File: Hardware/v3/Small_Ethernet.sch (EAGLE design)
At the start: 56 parts, among them U1 EDISON_CONNECTOR_FULLMOUNTING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, U2 LAN9512-JZX, U3 MAX4995AAUT+, U4 EDISON_CONNECTOR_FULLHEADER, X1 J1011F01P

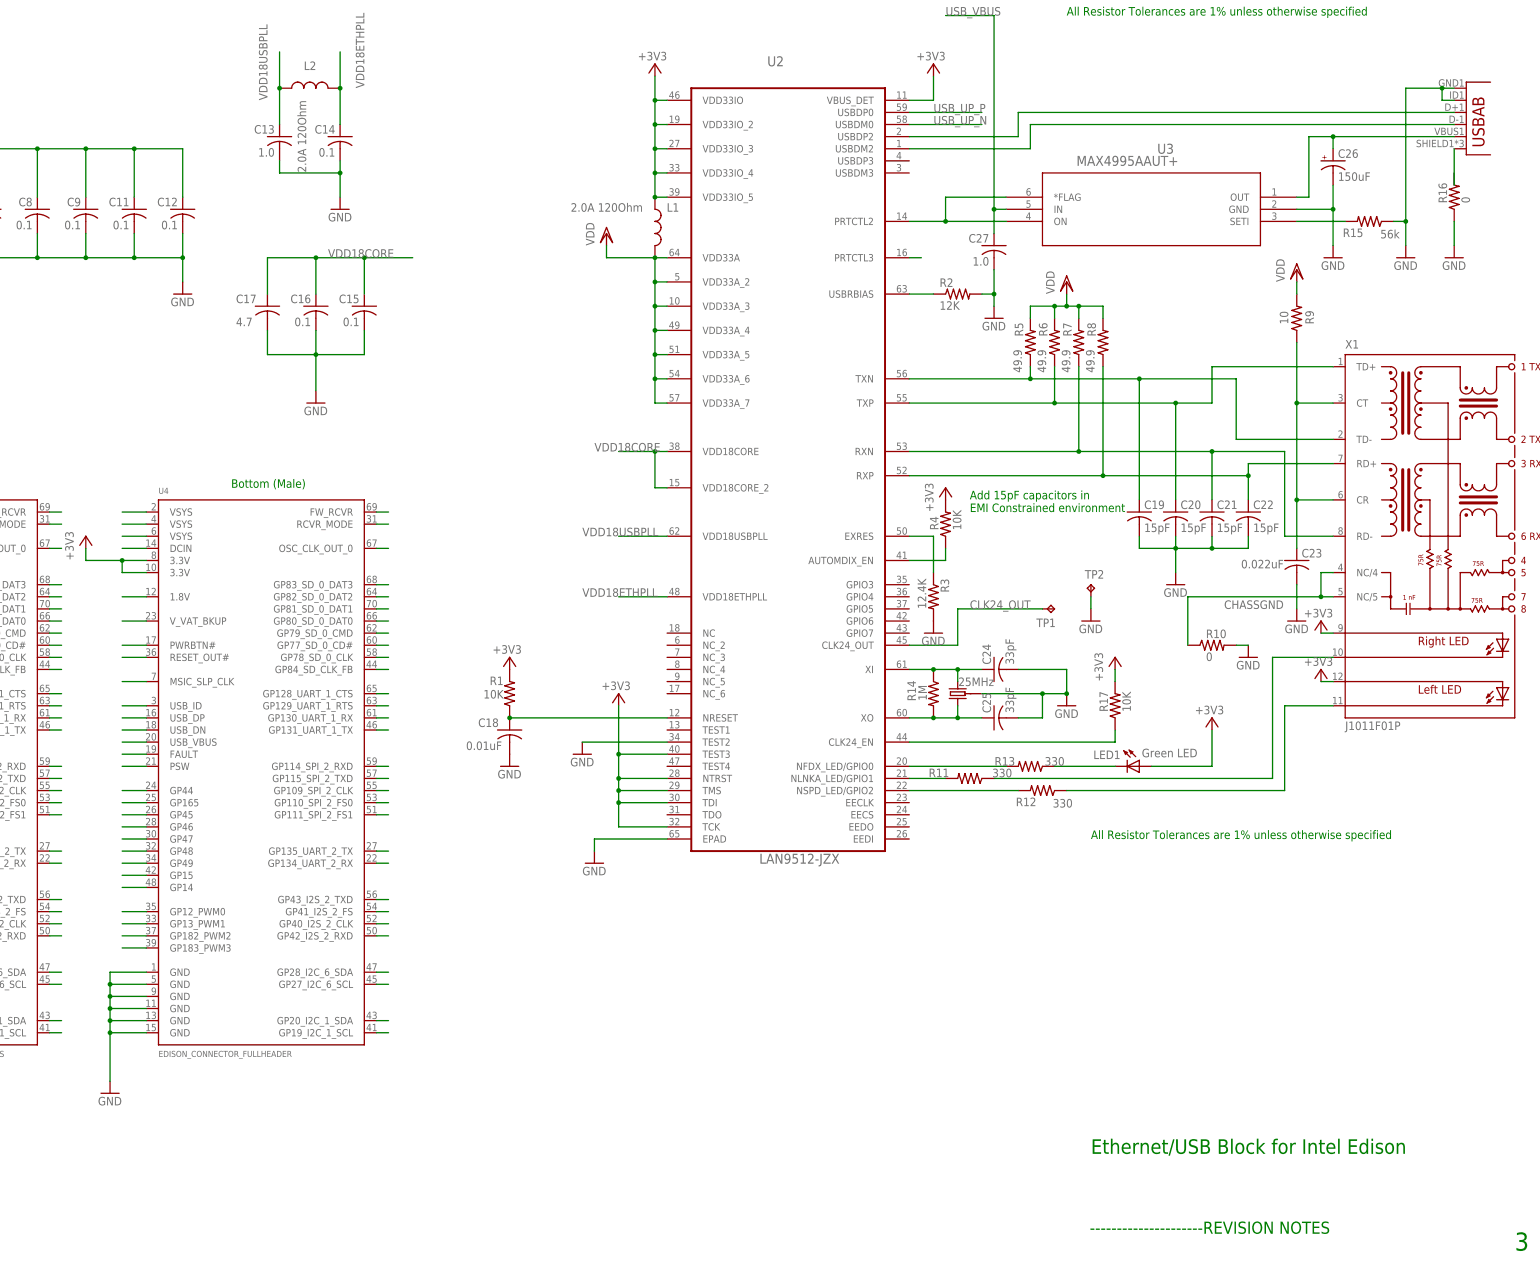
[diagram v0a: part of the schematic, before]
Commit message: Added ground fills. PoE: power planes around U7, diode for power through microB. Small: changed C26 to 2 caps, removed NP caps, removed test points, replaced crystal
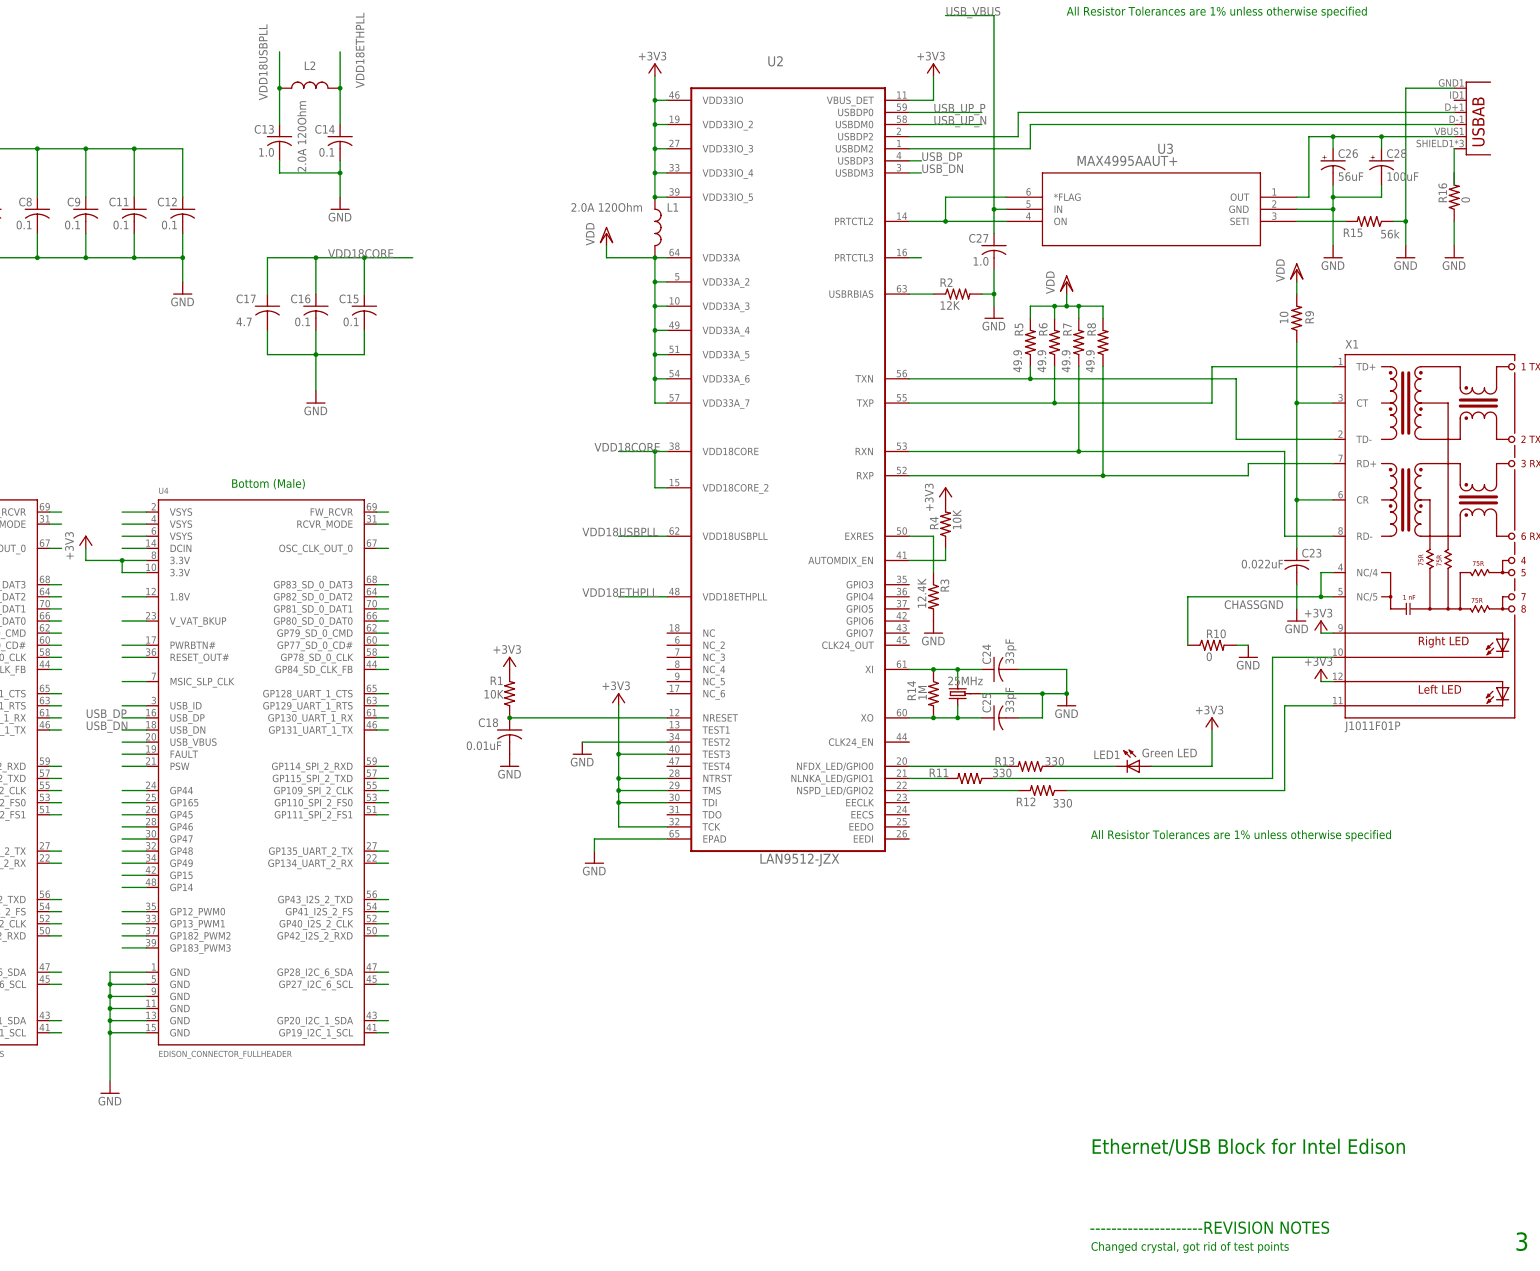
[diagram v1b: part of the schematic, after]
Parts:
- removed C19, C20, C21, C22: 15pF, rcl:C-USC0402
- removed R17: 10K, resistor:R-US_R0603
- removed TP1, TP2: TPTP20R, testpad:TPTP20R
- added C28: 100uF, PoEdev:EEF-CXXXXXXX
- C26: value 150uF -> 56uF; device SparkFun-Capacitors:CAP_POLE -> PoEdev:EEF-CXXXXXXX
- U$1: device SparkFun-FreqCtrl:CRYSTAL-GROUNDED -> PoEdev:CRYSTAL-ESC-32
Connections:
- removed net CLK24_OUT: TP1.TP, U2.CLK24_OUT
- removed net N$1: R17.1, U2.CLK24_EN
- removed net USBUP: U4.USB_DP
- removed net USBUP2: U4.USB_DN
- new net USB_DN: U2.USBDM3, U4.USB_DN
- new net USB_DP: U2.USBDP3, U4.USB_DP
- net +3V3: no longer R17.2
- net GND: now also C28.-; no longer C19.2, C20.2, C21.2, C22.2, JP1.USBID, TP2.TP
- net N$25: now also C28.+
- net RX_N: no longer C22.1
- net RX_P: no longer C21.1
- net TX_N: no longer C19.1
- net TX_P: no longer C20.1
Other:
- note added: "Changed crystal, got rid of test points"
- note removed: "Add 15pF capacitors in EMI Constrained environment"

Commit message: Added LDO for power off VSYS (to ensure enough current to LAN); Added datasheets for LDO and FTDI chip
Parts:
- added C19: 0.1uF, SparkFun-Capacitors:0.1UF-16V(+-10%)(0402)
- added C20, C21: 1.0uF, SparkFun-Capacitors:1.0UF-16V-10%(0402)
- added U5: MIC5353-3.3YMT, PoEdev:MIC5353-XXYMT
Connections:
- removed net P2: U1.VSYS@1, U4.VSYS@1
- removed net P4: U1.VSYS@2, U4.VSYS@2
- removed net P6: U1.VSYS@3, U4.VSYS@3
- new net ED3V: U1.3.3V@1, U1.3.3V@2, U4.3.3V@1, U4.3.3V@2
- new net N$1: C19.1, U5.BYP
- new net VCC: C20.2, U1.VSYS@1, U1.VSYS@2, U1.VSYS@3, U4.VSYS@1, U4.VSYS@2, U4.VSYS@3, U5.EN
- net +3V3: now also C21.2, U5.VOUT; no longer U1.3.3V@1, U1.3.3V@2, U4.3.3V@1, U4.3.3V@2
- net GND: now also C19.2, C20.1, C21.1, U5.GND
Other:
- note added: "3.2"
- note added: "Added LDO for power off VSYS"
- note removed: "3"
- note removed: "Changed crystal, got rid of test points"
